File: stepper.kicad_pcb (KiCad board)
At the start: 2 copper layers, 71.1 x 100.3 mm, 89 parts, among them IC1 PC817, IC2 PC817, IC3 PC817, IC4 PC817, IC5 PC817, IC6 PC817, K1 Delay Selector, P1 CONN_2, P2 CONN_8, P3 CONN_4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

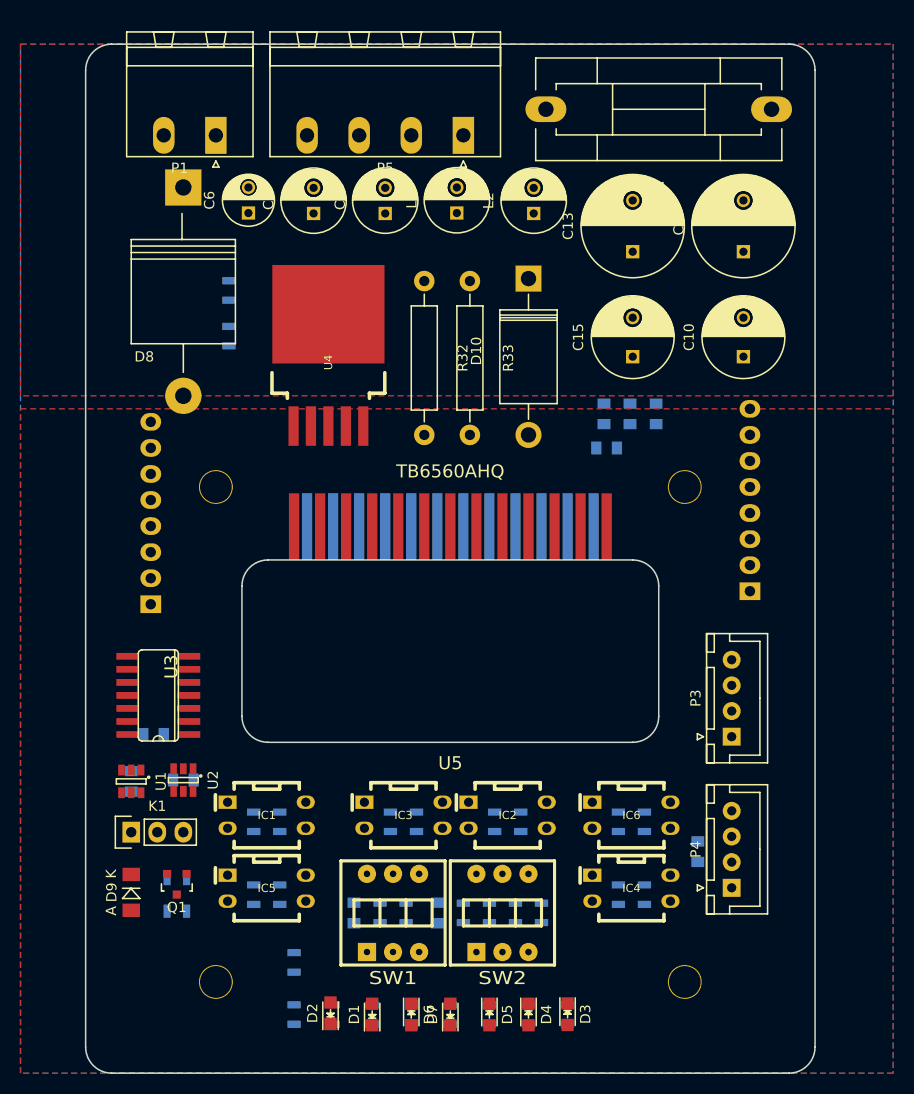
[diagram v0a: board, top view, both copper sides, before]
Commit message: adjust board, change lm2576 package
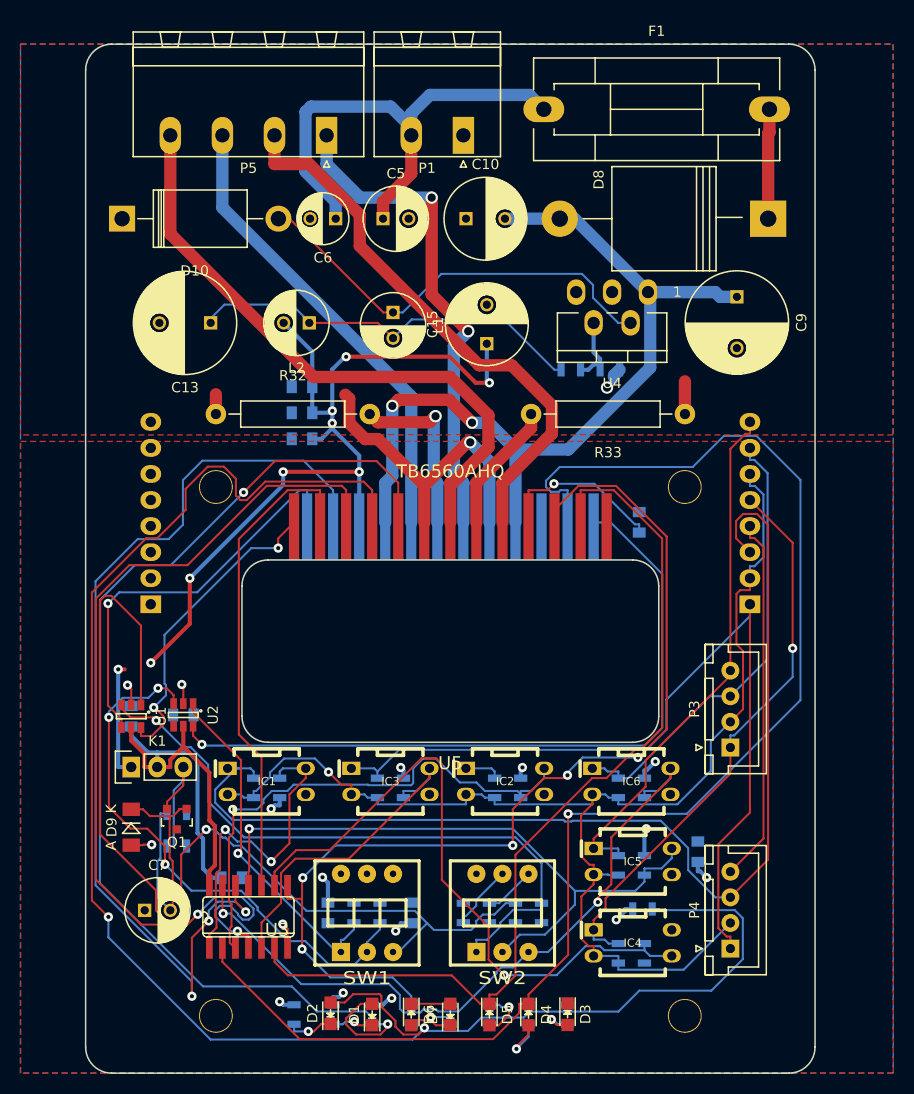
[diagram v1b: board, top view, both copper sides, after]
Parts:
- U4: footprint I20:TO-263-5 -> TO_SOT_Packages_THT:Pentawatt_Neutral_Staggered_Verical_TO220-5-T05D
- moved C7 71.9 mm to (145.5, 102.2), turned to 0 degrees
- moved D8 57.1 mm to (206.2, 34.8), turned to 180 degrees
- moved C13 41.7 mm to (151.9, 45.0), turned to 180 degrees
- moved D10 40.0 mm to (143.3, 34.8), turned to 0 degrees
- moved R31 37.3 mm to (190.8, 49.5), turned to 0 degrees
- moved IC5 35.8 mm to (193.0, 97.5)
- moved R18 35.7 mm to (191.6, 97.9)
- moved R25 35.7 mm to (194.2, 97.9)
- moved C18 34.6 mm to (160.8, 56.3), turned to 180 degrees
- moved R6 34.4 mm to (194.0, 102.1), turned to 0 degrees
- moved R30 34.2 mm to (187.0, 49.5), turned to 0 degrees
- moved C16 32.0 mm to (160.8, 53.7), turned to 180 degrees
- moved C10 30.2 mm to (176.8, 34.8), turned to 0 degrees
- moved C17 29.6 mm to (160.8, 51.2), turned to 180 degrees
- moved U4 27.8 mm to (191.0, 45.8), turned to 180 degrees
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- renumbered H2 to H1, H2 to H3, H2 to H4
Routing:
- net PROTECT: track 0.00 -> 169.5 mm, vias 0 -> 2
- net ENABLE: track 0.00 -> 139.6 mm, vias 0 -> 1
- net ExtGnd: track 0.00 -> 127.5 mm, vias 0 -> 1
- net VDD: track 0.00 -> 118.1 mm, vias 0 -> 21
- net MO: track 0.00 -> 110.0 mm, vias 0 -> 2
- net ExtENABLE: track 0.00 -> 108.4 mm
- net RESET: track 0.00 -> 100.7 mm, vias 0 -> 5
- net D1IN: track 0.00 -> 98.0 mm, vias 0 -> 1
- net M2: track 0.00 -> 95.7 mm, vias 0 -> 3
- net CLK: track 0.00 -> 90.9 mm
- net DIR: track 0.00 -> 89.7 mm, vias 0 -> 2
- net ExtCLK: track 0.00 -> 84.3 mm
- net HVDD: track 0.00 -> 82.7 mm, vias 0 -> 2
- net TQ1: track 0.00 -> 71.5 mm, vias 0 -> 1
- net M2_CTL: track 0.00 -> 69.5 mm, vias 0 -> 2
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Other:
- net class HCurrent: via_dia 0.9 -> 1.2; via_drill 0.4 -> 0.8

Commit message: add screenshot
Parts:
- U4: footprint TO_SOT_Packages_THT:Pentawatt_Neutral_Staggered_Verical_TO220-5-T05D -> I20:Pentawatt_Neutral_Staggered_Verical_TO220-5-T05D
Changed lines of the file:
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@@
     (links 190)
     (no_connects 32)
-    (area 133.35 14.0125 218.440001 119.1145)
+    (area 139.624999 17.704999 210.895001 118.185001)
     (thickness 1.6)
     (drawings 8)
@@
     (add_net VDD)
   )
+  (module I20:Pentawatt_Neutral_Staggered_Verical_TO220-5-T05D locked (layer F.Cu)
+    (at 191.031 45.7581 180)
+    (descr "Pentawatt, Neutral, Staggered, Verical, TO220-5, T05D,")
+    (tags "Pentawatt, Neutral, Staggered, Verical, TO220-5, T05D,")
+    (fp_text reference U4 (at 0 -5.08 180) (layer F.SilkS)
+      (effects (font (size 1 1) (thickness 0.15)))
+    )
+    (fp_text value LM2576HV (at 1.27 7.62 180) (layer F.Fab)
+      (effects (font (size 1 1) (thickness 0.15)))
+    )
+    (fp_text user 1 (at -6.35 3.81 180) (layer F.SilkS)
+      (effects (font (size 1 1) (thickness 0.15)))
+    )
+    (fp_line (start 3.302 1.778) (end 5.334 1.778) (layer F.SilkS) (width 0.15))
+    (fp_line (start -0.508 1.778) (end 0.508 1.778) (layer F.SilkS) (width 0.15))
+    (fp_line (start -5.334 1.778) (end -3.429 1.778) (layer F.SilkS) (width 0.15))
+    (fp_line (start -1.524 -3.048) (end -1.524 -1.905) (layer F.SilkS) (width 0.15))
+    (fp_line (start 1.524 -3.048) (end 1.524 -1.905) (layer F.SilkS) (width 0.15))
+    (fp_line (start 5.334 -1.905) (end 5.334 1.778) (layer F.SilkS) (width 0.15))
+    (fp_line (start -5.334 1.778) (end -5.334 -1.905) (layer F.SilkS) (width 0.15))
+    (fp_line (start 5.334 -3.048) (end 5.334 -1.905) (layer F.SilkS) (width 0.15))
+    (fp_line (start 5.334 -1.905) (end -5.334 -1.905) (layer F.SilkS) (width 0.15))
+    (fp_line (start -5.334 -1.905) (end -5.334 -3.048) (layer F.SilkS) (width 0.15))
+    (fp_line (start 0 -3.048) (end -5.334 -3.048) (layer F.SilkS) (width 0.15))
+    (fp_line (start 0 -3.048) (end 5.334 -3.048) (layer F.SilkS) (width 0.15))
+    (pad 3 thru_hole oval (at 0 3.79984 270) (size 2.49936 1.80086) (drill 1.19888) (layers *.Cu *.Mask F.SilkS)
+      (net 13 PGndA))
+    (pad 1 thru_hole oval (at -3.50012 3.79984 270) (size 2.49936 1.80086) (drill 1.19888) (layers *.Cu *.Mask F.SilkS)
+      (net 15 HVDD))
+    (pad 5 thru_hole oval (at 3.50012 3.79984 270) (size 2.49936 1.80086) (drill 1.19888) (layers *.Cu *.Mask F.SilkS)
+      (net 13 PGndA))
+    (pad 4 thru_hole oval (at 1.80086 0.8001 270) (size 2.49936 1.80086) (drill 1.19888) (layers *.Cu *.Mask F.SilkS)
+      (net 45 FEEDBACK))
+    (pad 2 thru_hole oval (at -1.80086 0.8001 270) (size 2.49936 1.80086) (drill 1.19888) (layers *.Cu *.Mask F.SilkS)
+      (net 51 "Net-(D10-Pad2)"))
+    (model ${I20}/shapes3D/TO/Pentawatt_Neutral_Staggered_Verical_TO220-5-T05D.wrl
+      (at (xyz 0 0 0))
+      (scale (xyz 0.3937 0.3937 0.3937))
+      (rotate (xyz 0 0 0))
+    )
+  )
   (module I20:MountingHole_3.1mm locked (layer F.Cu)
     (at 152.4 112.522)
@@
     )
   )
-  (module TO_SOT_Packages_THT:Pentawatt_Neutral_Staggered_Verical_TO220-5-T05D locked (layer F.Cu)
-    (at 191.031 45.7581 180)
-    (descr "Pentawatt, Neutral, Staggered, Verical, TO220-5, T05D,")
-    (tags "Pentawatt, Neutral, Staggered, Verical, TO220-5, T05D,")
-    (fp_text reference U4 (at 0 -5.08 180) (layer F.SilkS)
-      (effects (font (size 1 1) (thickness 0.15)))
-    )
-    (fp_text value LM2576HV (at 1.27 7.62 180) (layer F.Fab)
-      (effects (font (size 1 1) (thickness 0.15)))
-    )
-    (fp_text user 1 (at -6.35 3.81 180) (layer F.SilkS)
-      (effects (font (size 1 1) (thickness 0.15)))
-    )
-    (fp_line (start 3.302 1.778) (end 5.334 1.778) (layer F.SilkS) (width 0.15))
-    (fp_line (start -0.508 1.778) (end 0.508 1.778) (layer F.SilkS) (width 0.15))
-    (fp_line (start -5.334 1.778) (end -3.429 1.778) (layer F.SilkS) (width 0.15))
-    (fp_line (start -1.524 -3.048) (end -1.524 -1.905) (layer F.SilkS) (width 0.15))
-    (fp_line (start 1.524 -3.048) (end 1.524 -1.905) (layer F.SilkS) (width 0.15))
-    (fp_line (start 5.334 -1.905) (end 5.334 1.778) (layer F.SilkS) (width 0.15))
-    (fp_line (start -5.334 1.778) (end -5.334 -1.905) (layer F.SilkS) (width 0.15))
-    (fp_line (start 5.334 -3.048) (end 5.334 -1.905) (layer F.SilkS) (width 0.15))
-    (fp_line (start 5.334 -1.905) (end -5.334 -1.905) (layer F.SilkS) (width 0.15))
-    (fp_line (start -5.334 -1.905) (end -5.334 -3.048) (layer F.SilkS) (width 0.15))
-    (fp_line (start 0 -3.048) (end -5.334 -3.048) (layer F.SilkS) (width 0.15))
-    (fp_line (start 0 -3.048) (end 5.334 -3.048) (layer F.SilkS) (width 0.15))
-    (pad 3 thru_hole oval (at 0 3.79984 270) (size 2.49936 1.80086) (drill 1.19888) (layers *.Cu *.Mask F.SilkS)
-      (net 13 PGndA))
-    (pad 1 thru_hole oval (at -3.50012 3.79984 270) (size 2.49936 1.80086) (drill 1.19888) (layers *.Cu *.Mask F.SilkS)
-      (net 15 HVDD))
-    (pad 5 thru_hole oval (at 3.50012 3.79984 270) (size 2.49936 1.80086) (drill 1.19888) (layers *.Cu *.Mask F.SilkS)
-      (net 13 PGndA))
-    (pad 4 thru_hole oval (at 1.80086 0.8001 270) (size 2.49936 1.80086) (drill 1.19888) (layers *.Cu *.Mask F.SilkS)
-      (net 45 FEEDBACK))
-    (pad 2 thru_hole oval (at -1.80086 0.8001 270) (size 2.49936 1.80086) (drill 1.19888) (layers *.Cu *.Mask F.SilkS)
-      (net 51 "Net-(D10-Pad2)"))
-    (model TO_SOT_Packages_THT.3dshapes/Pentawatt_Neutral_Staggered_Verical_TO220-5-T05D.wrl
-      (at (xyz 0 0 0))
-      (scale (xyz 0.3937 0.3937 0.3937))
-      (rotate (xyz 0 0 0))
-    )
-  )
